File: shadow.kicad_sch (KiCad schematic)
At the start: 10 parts, among them U1 Arduino Nano 33 IoT

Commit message: feat: finish up control circut
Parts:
- added SW1, SW2: SW_Push, symbol Switch:SW_Push
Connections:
- net at MC1. (S2), U1.19 (GND): now also SW1.2, SW2.2
- net at U3.1 (OUT): no longer U1.6 (A2)
- net GND: now reaches U1.14 (GND), U1.3 (GND), U2.3 (GND), U3.3 (GND), U4.3 (GND), U5.3 (GND), U6.3 (GND), U7.3 (GND)
- net GND: now also OLED1. (VCC)
- net at U7.1 (OUT): no longer U1.10 (A6)
- net at U2.1 (OUT): no longer U1.5 (A1)
- net at U1.1 (D13): now also OLED1. (VCC)
- net at U1.20 (D2): now also SW1.1
- net at U1.21 (D3/PWM): now also SW2.1
- net at U1.30 (D12/MISO): now also OLED1. (VCC)
- net at U1.4 (A0/DAC0): no longer U1.1 (OUT)
- net at U1.7 (A3): no longer U4.1 (OUT)
- net at U1.8 (A4/SDA): no longer U5.1 (OUT)
- net at U1.9 (A5/SCL): no longer U6.1 (OUT)
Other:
- note added: "Jan 4 2025"
- note added: "Project Shadow"
- note added: "Shadow v0"
- note added: "Shenanigans are afoot :)"
- note added: "v0.0.1"
- note removed: "Shadow"
- note removed: "TODO: need vrm + lipo"
- moved on the sheet: MC1, OLED1, U1, U2, U3, U4, U5, U6, U7

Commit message: finish circut
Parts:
- removed MC1: ~, symbol Custom:FT-SMC-2CH
- renumbered U1 to S1, U2 to S2, U3 to S3, U4 to S4, U5 to S5, U6 to S6, U7 to S7
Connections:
- net GND: now also SW1.2, SW2.2, U1.19 (GND)
- net MC1_S1: now reaches U1.27 (D9/PWM)
- net MC1_S1: now also U1.28 (D10/PWM)
- net +5V renamed battery/5V
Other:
- added sheet battery (battery.kicad_sch)
- note added: "Shadow"
- note removed: "AA batteries (shenanigans maybe? boost buck maybe?)"
- note removed: "Jan 4 2025"
- note removed: "Project Shadow"
- note removed: "Shadow v0"
- note removed: "v0.0.1"
- company: (none) -> York Mills Collegiate Institute
- title: (none) -> Shadow
- moved on the sheet: OLED1, S1, S2, S3, S4, S5, S6, S7, SW1, SW2, U1

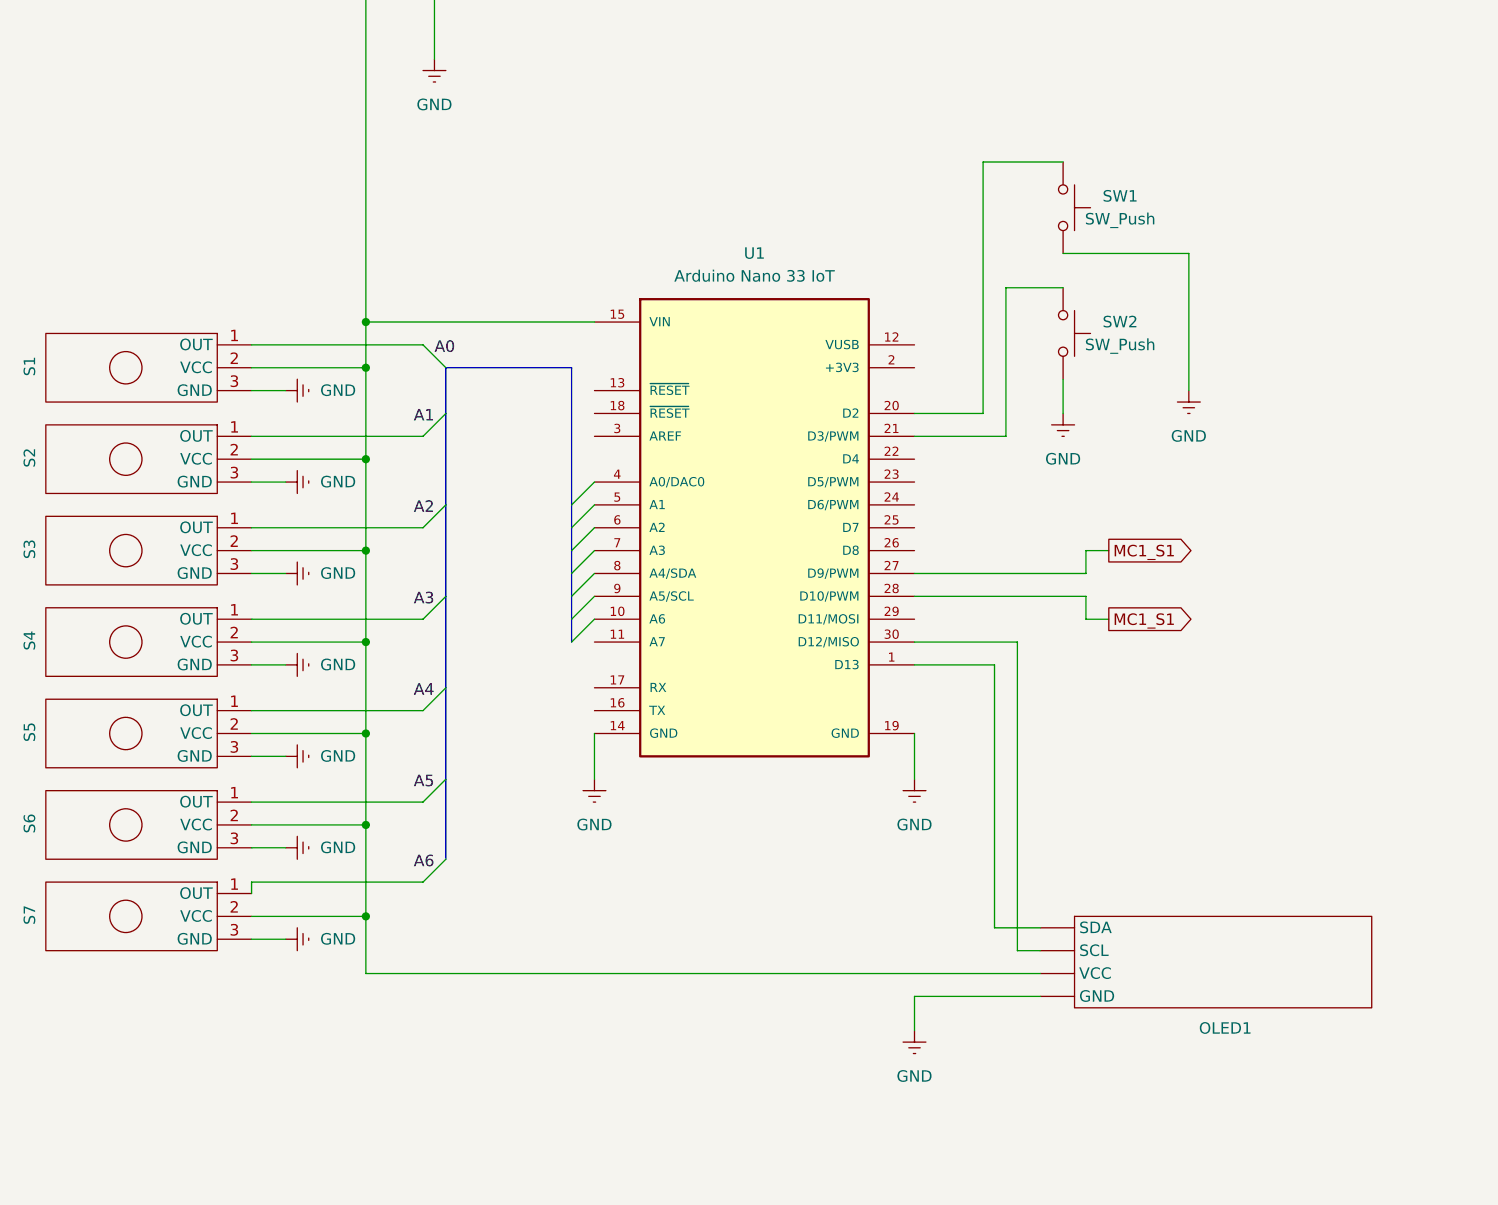
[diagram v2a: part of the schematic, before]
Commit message: chore: replace sensors with labels
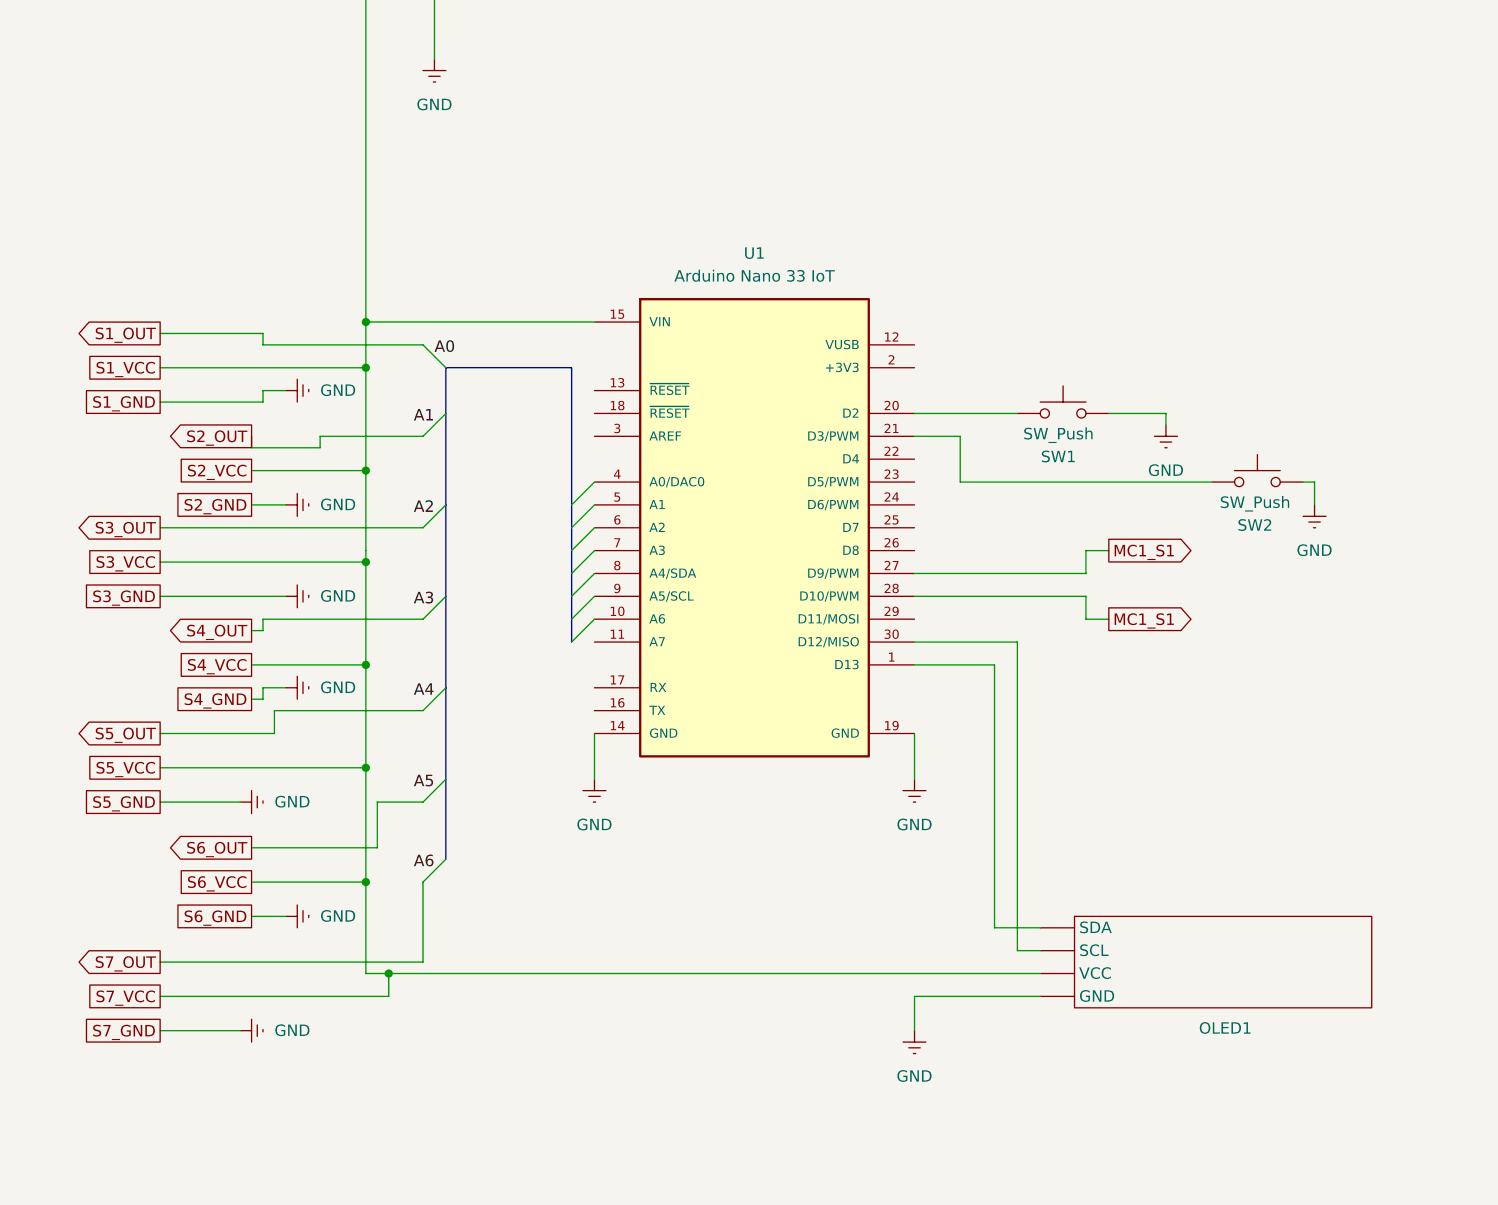
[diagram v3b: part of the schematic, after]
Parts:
- removed S1, S2, S3, S4, S5, S6, S7: ~, symbol Custom:SEN-11769
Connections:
- net battery/5V renamed S1_VCC
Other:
- moved on the sheet: SW1, SW2

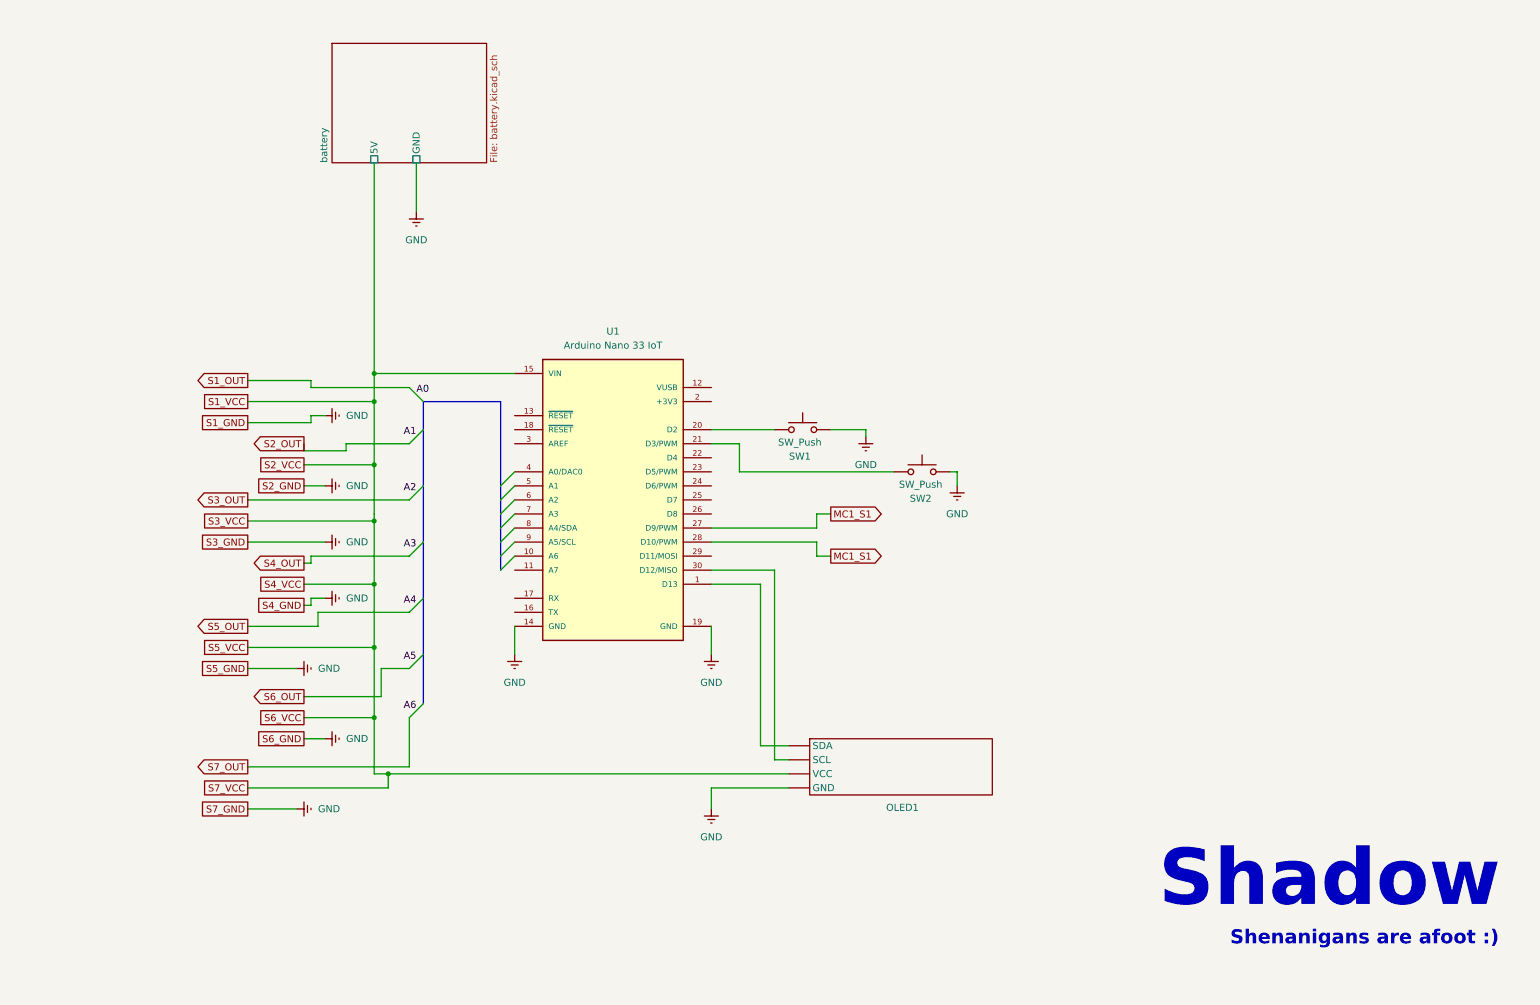
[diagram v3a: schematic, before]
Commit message: start work on i2c multiplexer
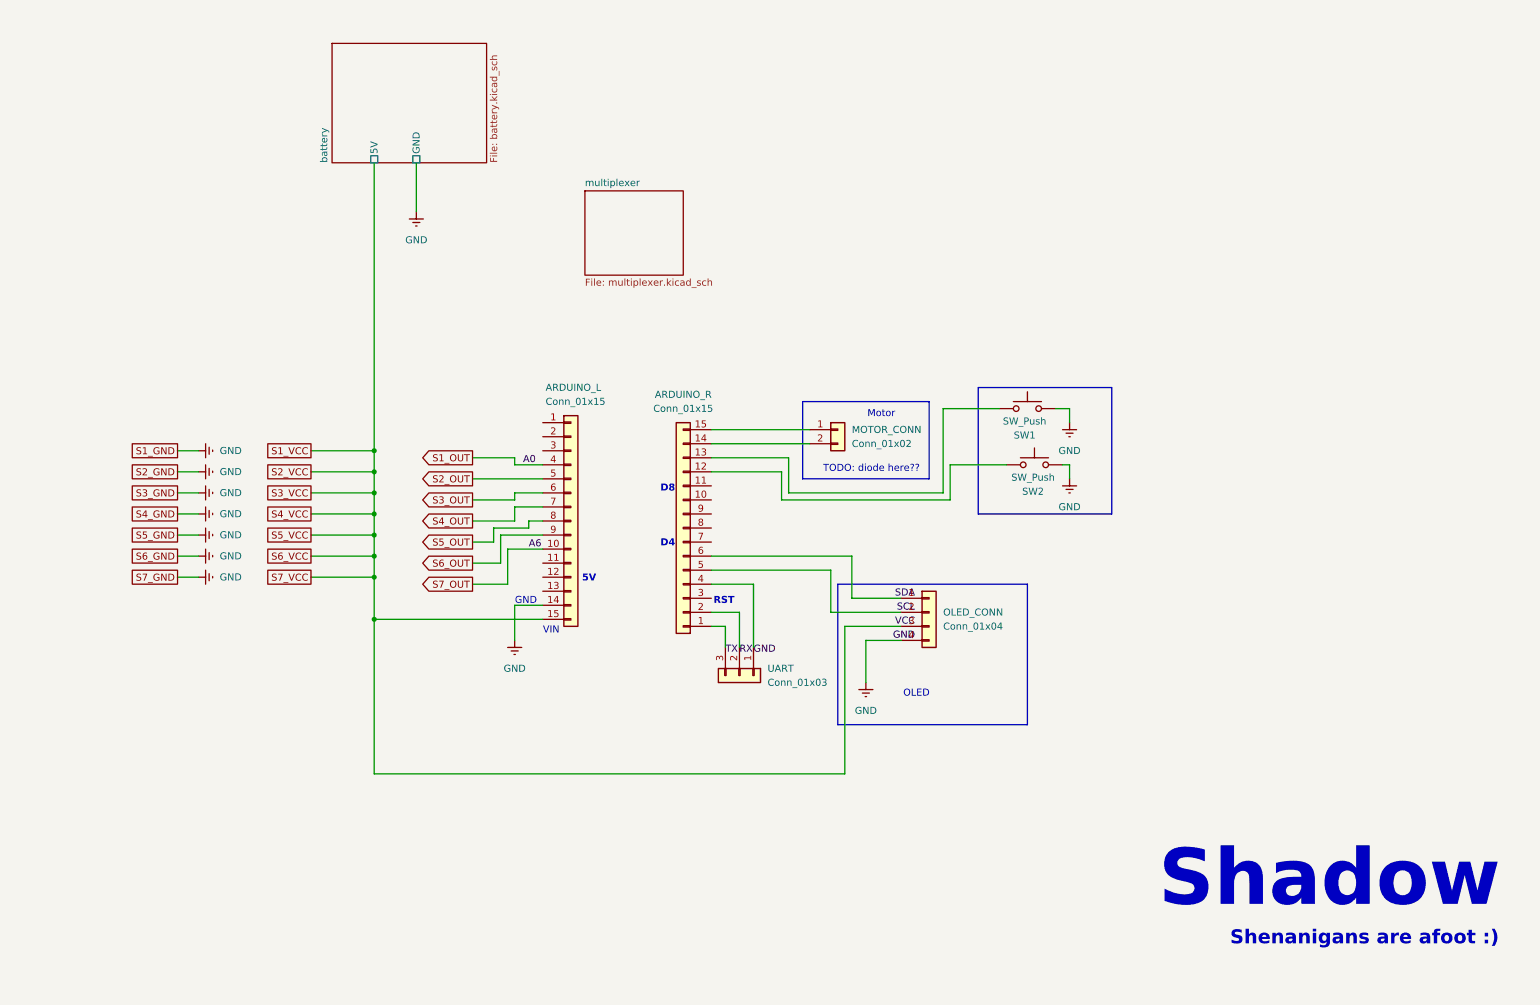
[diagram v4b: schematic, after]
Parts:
- removed OLED1: ~, symbol Custom:OLED
- removed U1: Arduino Nano 33 IoT, ABX00027:MODULE_ABX00027, symbol ABX00027:ABX00027
- added ARDUINO_L, ARDUINO_R: Conn_01x15, symbol Connector_Generic:Conn_01x15
- added MOTOR_CONN: Conn_01x02, symbol Connector_Generic:Conn_01x02
- added OLED_CONN: Conn_01x04, symbol Connector_Generic:Conn_01x04
- added UART: Conn_01x03, symbol Connector_Generic:Conn_01x03
- SW1, SW2: footprint (none) -> Button_Switch_THT:SW_PUSH-12mm
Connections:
- net GND: now also ARDUINO_L.14 (Pin_14), OLED_CONN.4 (Pin_4)
- net S1_OUT: now also ARDUINO_L.4 (Pin_4)
- net S1_VCC: now also ARDUINO_L.15 (Pin_15), OLED_CONN.3 (Pin_3)
- net S2_OUT: now also ARDUINO_L.5 (Pin_5)
- net S3_OUT: now also ARDUINO_L.6 (Pin_6)
- net S4_OUT: now also ARDUINO_L.7 (Pin_7)
- net S5_OUT: now also ARDUINO_L.8 (Pin_8)
- net S6_OUT: now also ARDUINO_L.9 (Pin_9)
- net S7_OUT: now also ARDUINO_L.10 (Pin_10)
- net at SW2.1: now also ARDUINO_R.12 (Pin_12)
- net at SW1.1: now also ARDUINO_R.13 (Pin_13)
- new net: ARDUINO_R.15 (Pin_15), MOTOR_CONN.1 (Pin_1)
- new net: ARDUINO_R.14 (Pin_14), MOTOR_CONN.2 (Pin_2)
- new net: ARDUINO_R.4 (Pin_4), UART.1 (Pin_1)
- new net: ARDUINO_R.2 (Pin_2), UART.2 (Pin_2)
- new net: ARDUINO_R.1 (Pin_1), UART.3 (Pin_3)
- new net: ARDUINO_R.6 (Pin_6), OLED_CONN.1 (Pin_1)
- new net: ARDUINO_R.5 (Pin_5), OLED_CONN.2 (Pin_2)
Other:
- added sheet multiplexer (multiplexer.kicad_sch)
- note added: "5V"
- note added: "D4"
- note added: "D8"
- note added: "GND"
- note added: "Motor"
- note added: "OLED"
- note added: "RST"
- note added: "TODO: diode here??"
- note added: "VIN"
- moved on the sheet: SW1, SW2

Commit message: FINISH SCHEMATICS
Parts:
- removed OLED_CONN: Conn_01x04, symbol Connector_Generic:Conn_01x04
- removed UART: Conn_01x03, symbol Connector_Generic:Conn_01x03
- added GPIO_L, GPIO_R: Conn_01x15, symbol Connector_Generic:Conn_01x15
- added OLED_CONN1, SENSOR_CONN, US_SENSOR_CONN: Conn_01x04, symbol Connector_Generic:Conn_01x04
- added RST_SW: SW_Push, Button_Switch_THT:SW_PUSH-12mm, symbol Switch:SW_Push
- added UART1: Conn_01x03, symbol Connector_Generic:Conn_01x03
- renumbered ARDUINO_L to PICO_L, ARDUINO_R to PICO_R
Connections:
- net S1_OUT is gone; now on net GPIO3: PICO_L.4 (Pin_4)
- net GND: now also PICO_L.13 (Pin_13), PICO_R.13 (Pin_13), GPIO_L.3 (Pin_3), GPIO_R.13 (Pin_13), OLED_CONN1.4 (Pin_4), RST_SW.2, SENSOR_CONN.4 (Pin_4), US_SENSOR_CONN.4 (Pin_4); no longer PICO_L.14 (Pin_14)
- net VCC: now also PICO_R.14 (Pin_14), GPIO_R.14 (Pin_14), OLED_CONN1.3 (Pin_3), SENSOR_CONN.3 (Pin_3), US_SENSOR_CONN.3 (Pin_3)
- net GPIO15: now reaches PICO_R.15 (Pin_15)
- net GPIO15: now also GPIO_R.15 (Pin_15); no longer MOTOR_CONN.1 (Pin_1)
- net GPIO3: now reaches MOTOR_CONN.2 (Pin_2)
- net GPIO3: now also GPIO_L.12 (Pin_12); no longer PICO_R.14 (Pin_14)
- net GPIO18: now reaches PICO_R.12 (Pin_12)
- net GPIO18: now also GPIO_R.12 (Pin_12); no longer SW2.1
- net GPIO26: now reaches PICO_R.4 (Pin_4)
- net GPIO26: now also GPIO_R.4 (Pin_4)
- net GPIO28: now reaches PICO_R.2 (Pin_2)
- net GPIO28: now also GPIO_R.2 (Pin_2)
- net GPIO29: now reaches PICO_R.1 (Pin_1)
- net GPIO29: now also GPIO_R.1 (Pin_1)
- net GPIO24: now reaches PICO_R.6 (Pin_6)
- net GPIO24: now also SW2.1, GPIO_R.6 (Pin_6)
- net GPIO25: now reaches PICO_R.5 (Pin_5)
- net GPIO25: now also GPIO_R.5 (Pin_5)
- net GPIO20: now reaches PICO_R.10 (Pin_10)
- net GPIO20: now also GPIO_R.10 (Pin_10), RST_SW.1
- net GPIO19: now reaches PICO_R.11 (Pin_11)
- net GPIO19: now also GPIO_R.11 (Pin_11)
- net GPIO23: now reaches SW1.1
- net GPIO23: now also PICO_R.7 (Pin_7), GPIO_R.7 (Pin_7); no longer PICO_R.13 (Pin_13)
- net GPIO27: now reaches PICO_R.3 (Pin_3)
- net GPIO27: now also GPIO_R.3 (Pin_3)
- net GPIO22: now reaches PICO_R.8 (Pin_8)
- net GPIO22: now also GPIO_R.8 (Pin_8)
- net GPIO21: now reaches PICO_R.9 (Pin_9)
- net GPIO21: now also GPIO_R.9 (Pin_9)
- net GPIO0: now reaches PICO_L.1 (Pin_1)
- net GPIO0: now also GPIO_L.15 (Pin_15), UART1.3 (Pin_3)
- net GPIO10: now reaches PICO_L.11 (Pin_11)
- net GPIO10: now also GPIO_L.5 (Pin_5)
- net GPIO11: now reaches PICO_L.12 (Pin_12)
- net GPIO11: now also GPIO_L.4 (Pin_4)
- net GPIO1: now reaches PICO_L.2 (Pin_2)
- net GPIO1: now also GPIO_L.14 (Pin_14), UART1.2 (Pin_2)
- net GPIO2: now reaches PICO_L.3 (Pin_3)
- net GPIO2: now also GPIO_L.13 (Pin_13), UART1.1 (Pin_1)
- net S1_VCC renamed GPIO14
- net GPIO14: now also GPIO_L.1 (Pin_1)
- net S2_OUT renamed GPIO4
- net GPIO4: now also MOTOR_CONN.1 (Pin_1), GPIO_L.11 (Pin_11)
- net S3_OUT renamed GPIO5
- net GPIO5: now also GPIO_L.10 (Pin_10)
- net S4_OUT renamed GPIO6
- net GPIO6: now also GPIO_L.9 (Pin_9)
- net S5_OUT renamed GPIO7
- net GPIO7: now also GPIO_L.8 (Pin_8)
- net S6_OUT renamed GPIO8
- net GPIO8: now also GPIO_L.7 (Pin_7)
- net S7_OUT renamed GPIO9
- net GPIO9: now also GPIO_L.6 (Pin_6)
- new net GPIO13: GPIO_L.2 (Pin_2), PICO_L.14 (Pin_14)
- new net OLED_SCL: OLED_CONN1.2 (Pin_2)
- new net OLED_SDA: OLED_CONN1.1 (Pin_1)
- new net SENSOR_SCL: SENSOR_CONN.2 (Pin_2)
- new net SENSOR_SDA: SENSOR_CONN.1 (Pin_1)
- new net US_SCL: US_SENSOR_CONN.2 (Pin_2)
- new net US_SDA: US_SENSOR_CONN.1 (Pin_1)
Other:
- added sheet I2C_PINOUT (I2C_PINOUT.kicad_sch)
- added sheet I2C_PINOUT1 (I2C_PINOUT.kicad_sch)
- added sheet I2C_PINOUT10 (I2C_PINOUT.kicad_sch)
- added sheet I2C_PINOUT11 (I2C_PINOUT.kicad_sch)
- added sheet I2C_PINOUT12 (I2C_PINOUT.kicad_sch)
- added sheet I2C_PINOUT2 (I2C_PINOUT.kicad_sch)
- added sheet I2C_PINOUT3 (I2C_PINOUT.kicad_sch)
- added sheet I2C_PINOUT4 (I2C_PINOUT.kicad_sch)
- added sheet I2C_PINOUT5 (I2C_PINOUT.kicad_sch)
- added sheet I2C_PINOUT6 (I2C_PINOUT.kicad_sch)
- added sheet I2C_PINOUT7 (I2C_PINOUT.kicad_sch)
- added sheet I2C_PINOUT8 (I2C_PINOUT.kicad_sch)
- added sheet I2C_PINOUT9 (I2C_PINOUT.kicad_sch)
- added sheet multiplexer1 (multiplexer.kicad_sch)
- sheet multiplexer ports: added GND, SC0, SC1, SC2, SC3, SC4, SC5, SC6, SC7, SCL_IN, SD0, SD1, SD2, SD3, SD4, SD5, SD6, SD7, SDA_IN, VIN; removed none
- note removed: "5V"
- note removed: "D4"
- note removed: "D8"
- note removed: "GND"
- note removed: "OLED"
- note removed: "RST"
- note removed: "VIN"
- moved on the sheet: MOTOR_CONN, PICO_R, SW1, SW2
